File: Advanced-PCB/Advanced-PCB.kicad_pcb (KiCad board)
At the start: 2 copper layers, 24 parts, among them J1 USB_mini_micro_B, SW1 MXSwitch, SW2 MXSwitch, SW3 MXSwitch, SW4 MXSwitch, U1 ATMEGA32U4, X1 16MHz

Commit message: PCB Layout Complete
Full PCB layed out in wanted order.
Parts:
- added D10: 1N4148W, Diode_SMD:D_SOD-123, F.Cu at (11.1, 25.7)
- added D11: 1N4148W, Diode_SMD:D_SOD-123, F.Cu at (11.1, 22.4)
- added D12: 1N4148W, Diode_SMD:D_SOD-123, F.Cu at (94.6, 124.8)
- added D13: 1N4148W, Diode_SMD:D_SOD-123, F.Cu at (20.1, 57.0)
- added D14: 1N4148W, Diode_SMD:D_SOD-123, F.Cu at (31.6, 69.4)
- added D15: 1N4148W, Diode_SMD:D_SOD-123, F.Cu at (25.9, 62.7)
- added D16: 1N4148W, Diode_SMD:D_SOD-123, F.Cu at (74.5, 116.4)
- added D17: 1N4148W, Diode_SMD:D_SOD-123, F.Cu at (31.6, 66.0)
- added D18: 1N4148W, Diode_SMD:D_SOD-123, F.Cu at (31.6, 62.7)
- added D19: 1N4148W, Diode_SMD:D_SOD-123, F.Cu at (25.9, 59.3)
- added D20: 1N4148W, Diode_SMD:D_SOD-123, F.Cu at (114.8, 144.9)
- added D21: 1N4148W, Diode_SMD:D_SOD-123, F.Cu at (83.1, 118.1)
- added D22: 1N4148W, Diode_SMD:D_SOD-123, F.Cu at (88.9, 124.8)
- added D23: 1N4148W, Diode_SMD:D_SOD-123, F.Cu at (88.9, 121.4)
- added D24: 1N4148W, Diode_SMD:D_SOD-123, F.Cu at (125.4, 158.4)
- added D25: 1N4148W, Diode_SMD:D_SOD-123, F.Cu at (131.2, 161.7)
- added D26: 1N4148W, Diode_SMD:D_SOD-123, F.Cu at (20.1, 53.6)
- added D27: 1N4148W, Diode_SMD:D_SOD-123, F.Cu at (114.8, 148.3)
- added D28: 1N4148W, Diode_SMD:D_SOD-123, F.Cu at (103.3, 138.2)
- added D29: 1N4148W, Diode_SMD:D_SOD-123, F.Cu at (109.0, 144.9)
- added D30: 1N4148W, Diode_SMD:D_SOD-123, F.Cu at (94.6, 131.5)
- added D31: 1N4148W, Diode_SMD:D_SOD-123, F.Cu at (83.1, 121.4)
- added D32: 1N4148W, Diode_SMD:D_SOD-123, F.Cu at (25.4, 50.3)
- added D33: 1N4148W, Diode_SMD:D_SOD-123, F.Cu at (114.8, 141.6)
- added D34: 1N4148W, Diode_SMD:D_SOD-123, F.Cu at (109.0, 138.2)
- added D35: 1N4148W, Diode_SMD:D_SOD-123, F.Cu at (136.9, 161.7)
- added D36: 1N4148W, Diode_SMD:D_SOD-123, F.Cu at (131.2, 158.4)
- added D37: 1N4148W, Diode_SMD:D_SOD-123, F.Cu at (94.6, 121.4)
- added D38: 1N4148W, Diode_SMD:D_SOD-123, F.Cu at (114.8, 138.2)
- added D39: 1N4148W, Diode_SMD:D_SOD-123, F.Cu at (31.6, 59.3)
- added D40: 1N4148W, Diode_SMD:D_SOD-123, F.Cu at (34.2, 76.1)
- added D41: 1N4148W, Diode_SMD:D_SOD-123, F.Cu at (25.9, 56.0)
- added D42: 1N4148W, Diode_SMD:D_SOD-123, F.Cu at (54.3, 96.3)
- added D43: 1N4148W, Diode_SMD:D_SOD-123, F.Cu at (31.6, 56.0)
- added D44: 1N4148W, Diode_SMD:D_SOD-123, F.Cu at (94.6, 118.1)
- added D45: 1N4148W, Diode_SMD:D_SOD-123, F.Cu at (142.7, 161.7)
- added D46: 1N4148W, Diode_SMD:D_SOD-123, F.Cu at (136.9, 158.4)
- added D47: 1N4148W, Diode_SMD:D_SOD-123, F.Cu at (11.1, 32.4)
- added D48: 1N4148W, Diode_SMD:D_SOD-123, F.Cu at (11.1, 29.1)
- added D49: 1N4148W, Diode_SMD:D_SOD-123, F.Cu at (165.7, 158.4)
- added D5: 1N4148W, Diode_SMD:D_SOD-123, F.Cu at (20.1, 60.3)
- added D50: 1N4148W, Diode_SMD:D_SOD-123, F.Cu at (142.7, 158.4)
- added D51: 1N4148W, Diode_SMD:D_SOD-123, F.Cu at (154.2, 161.7)
- added D52: 1N4148W, Diode_SMD:D_SOD-123, F.Cu at (148.4, 158.4)
- added D53: 1N4148W, Diode_SMD:D_SOD-123, F.Cu at (11.1, 19.0)
- added D54: 1N4148W, Diode_SMD:D_SOD-123, F.Cu at (11.1, 15.7)
- added D55: 1N4148W, Diode_SMD:D_SOD-123, F.Cu at (154.2, 158.4)
- added D56: 1N4148W, Diode_SMD:D_SOD-123, F.Cu at (159.9, 161.7)
- added D57: 1N4148W, Diode_SMD:D_SOD-123, F.Cu at (165.7, 161.7)
- added D58: 1N4148W, Diode_SMD:D_SOD-123, F.Cu at (159.9, 158.4)
- added D59: 1N4148W, Diode_SMD:D_SOD-123, F.Cu at (148.4, 161.7)
- added D6: 1N4148W, Diode_SMD:D_SOD-123, F.Cu at (88.9, 128.1)
- added D60: 1N4148W, Diode_SMD:D_SOD-123, F.Cu at (181.1, 79.4)
- added D61: 1N4148W, Diode_SMD:D_SOD-123, F.Cu at (181.1, 76.0)
- added D62: 1N4148W, Diode_SMD:D_SOD-123, F.Cu at (181.1, 72.7)
- added D63: 1N4148W, Diode_SMD:D_SOD-123, F.Cu at (166.9, 52.2)
- added D64: 1N4148W, Diode_SMD:D_SOD-123, F.Cu at (181.1, 69.3)
- added D65: 1N4148W, Diode_SMD:D_SOD-123, F.Cu at (88.9, 118.1)
- added D66: 1N4148W, Diode_SMD:D_SOD-123, F.Cu at (109.0, 141.6)
- added D67: 1N4148W, Diode_SMD:D_SOD-123, F.Cu at (19.6, 50.3)
- added D7: 1N4148W, Diode_SMD:D_SOD-123, F.Cu at (94.6, 128.1)
- added D8: 1N4148W, Diode_SMD:D_SOD-123, F.Cu at (94.6, 134.8)
- added D9: 1N4148W, Diode_SMD:D_SOD-123, F.Cu at (172.7, 52.2)
- added SW10: Win 1.25, acheron_MXH:MX125H, B.Cu at (-11.9, -28.6)
- added SW11: 2, acheron_MXH:MX100H, B.Cu at (0.00, -104.8)
- added SW12: W, acheron_MXH:MX100H, B.Cu at (9.53, -85.7)
- added SW13: S, acheron_MXH:MX100H, B.Cu at (14.3, -66.7)
- added SW14: X, acheron_MXH:MX100H, B.Cu at (23.8, -47.6)
- added SW15: Alt 1.25, acheron_MXH:MX125H, B.Cu at (11.9, -28.6)
- added SW16: 3, acheron_MXH:MX100H, B.Cu at (19.1, -104.8)
- added SW17: E, acheron_MXH:MX100H, B.Cu at (28.6, -85.7)
- added SW18: D, acheron_MXH:MX100H, B.Cu at (33.3, -66.7)
- added SW19: C, acheron_MXH:MX100H, B.Cu at (42.9, -47.6)
- added SW20: 4, acheron_MXH:MX100H, B.Cu at (38.1, -104.8)
- added SW21: R, acheron_MXH:MX100H, B.Cu at (47.6, -85.7)
- added SW22: F, acheron_MXH:MX100H, B.Cu at (52.4, -66.7)
- added SW23: V, acheron_MXH:MX100H, B.Cu at (61.9, -47.6)
- added SW24: 5, acheron_MXH:MX100H, B.Cu at (57.1, -104.8)
- added SW25: T, acheron_MXH:MX100H, B.Cu at (66.7, -85.7)
- added SW26: G, acheron_MXH:MX100H, B.Cu at (71.4, -66.7)
- added SW27: B, acheron_MXH:MX100H, B.Cu at (81.0, -47.6)
- added SW28: Space 6.25, acheron_MXH:MX625HR, B.Cu at (83.3, -28.6)
- added SW29: 6, acheron_MXH:MX100H, B.Cu at (76.2, -104.8)
- added SW30: Y, acheron_MXH:MX100H, B.Cu at (85.7, -85.7)
- added SW31: H, acheron_MXH:MX100H, B.Cu at (90.5, -66.7)
- added SW32: N, acheron_MXH:MX100H, B.Cu at (100.0, -47.6)
- added SW33: 7, acheron_MXH:MX100H, B.Cu at (95.2, -104.8)
- added SW34: U, acheron_MXH:MX100H, B.Cu at (104.8, -85.7)
- added SW35: J, acheron_MXH:MX100H, B.Cu at (109.5, -66.7)
- added SW36: M, acheron_MXH:MX100H, B.Cu at (119.1, -47.6)
- added SW37: 8, acheron_MXH:MX100H, B.Cu at (114.3, -104.8)
- added SW38: I, acheron_MXH:MX100H, B.Cu at (123.8, -85.7)
- added SW39: K, acheron_MXH:MX100H, B.Cu at (128.6, -66.7)
- added SW40: ,, acheron_MXH:MX100H, B.Cu at (138.1, -47.6)
- added SW41: 9, acheron_MXH:MX100H, B.Cu at (133.3, -104.8)
- added SW42: O, acheron_MXH:MX100H, B.Cu at (161.9, -85.7)
- added SW43: L, acheron_MXH:MX100H, B.Cu at (147.6, -66.7)
- added SW44: ., acheron_MXH:MX100H, B.Cu at (157.2, -47.6)
- added SW45: Alt 1.25, acheron_MXH:MX125H, B.Cu at (154.8, -28.6)
- added SW46: 0, acheron_MXH:MX100H, B.Cu at (152.4, -104.8)
- added SW47: P, acheron_MXH:MX100H, B.Cu at (142.9, -85.7)
- added SW48: ;, acheron_MXH:MX100H, B.Cu at (166.7, -66.7)
- added SW49: /, acheron_MXH:MX100H, F.Cu at (176.2, -47.6)
- added SW5: Ctrl 1.25, acheron_MXH:MX125H, B.Cu at (-35.7, -28.6)
- added SW50: Fn 1.25, acheron_MXH:MX125H, B.Cu at (178.6, -28.6)
- added SW51: -, acheron_MXH:MX100H, B.Cu at (171.4, -104.8)
- added SW52: [, acheron_MXH:MX100H, B.Cu at (181.0, -85.7)
- added SW53: ', acheron_MXH:MX100H, B.Cu at (185.7, -66.7)
- added SW54: Shift 1.75, acheron_MXH:MX175H, B.Cu at (202.4, -47.6)
- added SW55: Left Arrow, acheron_MXH:MX100H, B.Cu at (209.6, -28.6)
- added SW56: =, acheron_MXH:MX100H, B.Cu at (190.5, -104.8)
- added SW57: ], acheron_MXH:MX100H, B.Cu at (200.0, -85.7)
- added SW58: Enter 2.25, acheron_MXH:MX225HR, B.Cu at (216.7, -66.7)
- added SW59: Up Arrow, acheron_MXH:MX100H, B.Cu at (228.6, -47.6)
- added SW6: 1, acheron_MXH:MX100H, B.Cu at (-19.1, -104.8)
- added SW60: Down Arrow, acheron_MXH:MX100H, B.Cu at (228.6, -28.6)
- added SW61: Back 2.00, acheron_MXH:MX200HR, B.Cu at (219.1, -104.8)
- added SW62: \ 1.50, acheron_MXH:MX150H, B.Cu at (223.8, -85.7)
- added SW63: Pg Up, acheron_MXH:MX100H, B.Cu at (247.7, -66.7)
- added SW64: Pg Down, acheron_MXH:MX100H, B.Cu at (247.7, -47.6)
- added SW65: Right Arrow, acheron_MXH:MX100H, B.Cu at (247.7, -28.6)
- added SW66: `, acheron_MXH:MX100H, B.Cu at (247.7, -104.8)
- added SW67: Del, acheron_MXH:MX100H, B.Cu at (247.7, -85.7)
- added SW7: Q, acheron_MXH:MX100H, B.Cu at (-9.53, -85.7)
- added SW8: A, acheron_MXH:MX100H, B.Cu at (-4.76, -66.7)
- added SW9: Z, acheron_MXH:MX100H, B.Cu at (4.76, -47.6)
- C1: value 22pF -> .1u
- C6: value .1u -> 4.7u
- C7: value 4.7u -> 22pF
- D1, D2, D3, D4: value D_Small -> 1N4148W
- R2: value 10k -> 22
- R4: value 22 -> 10k
- SW1: value MXSwitch -> Esc; moved to B.Cu
- SW2: value MXSwitch -> Tab 1.50; footprint acheron_MXH:MX100H -> acheron_MXH:MX150H; moved to B.Cu
- SW3: value MXSwitch -> Caps 1.75; footprint acheron_MXH:MX100H -> acheron_MXH:MX175H; moved to B.Cu
- SW4: value MXSwitch -> Shift 2.25; footprint acheron_MXH:MX100H -> acheron_MXH:MX225HR; moved to B.Cu
- moved SW1 182.5 mm to (-38.1, -104.8), turned to 180 degrees
- moved SWPw1 158.4 mm to (173.3, 160.2), turned to 180 degrees
- moved SW2 147.4 mm to (-33.3, -85.7), turned to 180 degrees
- moved C6 144.9 mm to (181.6, 82.5), turned to 180 degrees
- moved D2 137.8 mm to (119.7, 158.4), turned to 180 degrees
- moved SW3 135.8 mm to (-31.0, -66.7), turned to 180 degrees
- moved C7 134.9 mm to (162.0, 43.5), turned to 180 degrees
- moved D1 130.1 mm to (125.4, 161.7), turned to 180 degrees
- moved C5 119.6 mm to (161.7, 49.4), turned to 180 degrees
- moved C4 114.6 mm to (161.7, 52.4), turned to 180 degrees
- moved R1 109.7 mm to (109.5, 148.1), turned to 180 degrees
- moved X1 101.7 mm to (180.6, 64.9), turned to 180 degrees
- moved SW4 100.5 mm to (-26.2, -47.6), turned to 180 degrees
- moved J1 86.1 mm to (170.0, 42.8), turned to 180 degrees
- moved R4 85.0 mm to (11.4, 44.4), turned to 180 degrees
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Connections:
- C1 pad 1: Net-(C1-Pad1) -> VCC
- C7 pad 1: VCC -> Net-(C7-Pad1)
- D3 pad 1: Net-(D3-Pad1) -> Col1
- R2 pad 1: +5V -> Net-(R2-Pad1)
- R2 pad 2: Net-(R2-Pad2) -> Net-(J1-Pad2)
- R3 pad 2: Net-(J1-Pad2) -> Net-(J1-Pad3)
- R4 pad 1: Net-(R4-Pad1) -> +5V
- R4 pad 2: Net-(J1-Pad3) -> Net-(R4-Pad2)
- SW1 pad 2: Net-(SW1-Pad2) -> Net-(D1-Pad2)
- U1 pad 16: Net-(C1-Pad1) -> Net-(C2-Pad1)
- U1 pad 17: Net-(C2-Pad1) -> Net-(C7-Pad1)
- U1 pad 3: Net-(R3-Pad1) -> Net-(R2-Pad1)
- U1 pad 33: Net-(R2-Pad2) -> Net-(R4-Pad2)
- U1 pad 4: Net-(R4-Pad1) -> Net-(R3-Pad1)
- X1 pad 1: Net-(C1-Pad1) -> Net-(C2-Pad1)
- X1 pad 2: Net-(C2-Pad1) -> Net-(C7-Pad1)

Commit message: Alternate Row 0
Alternate Row zero with 1u right side keys added.
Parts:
- SW49: moved to B.Cu
- moved J1 165.8 mm to (104.8, -109.6)
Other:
- board outline added: 309.6 x 100 mm

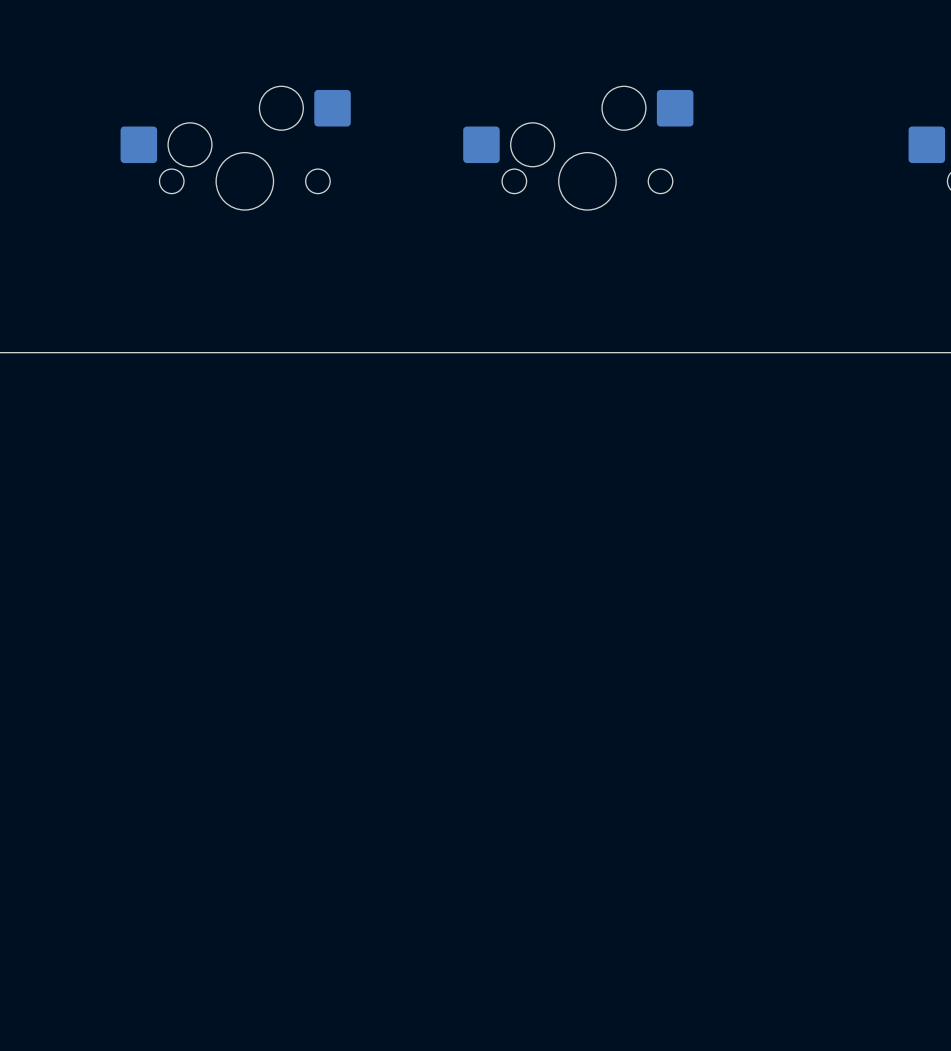
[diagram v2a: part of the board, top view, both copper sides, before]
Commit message: Layout Simplified
Layout Simplified by stacking switches unable to be used at same time because of different kb layouts. Right alt and fn with ctrl left down as seperate row.
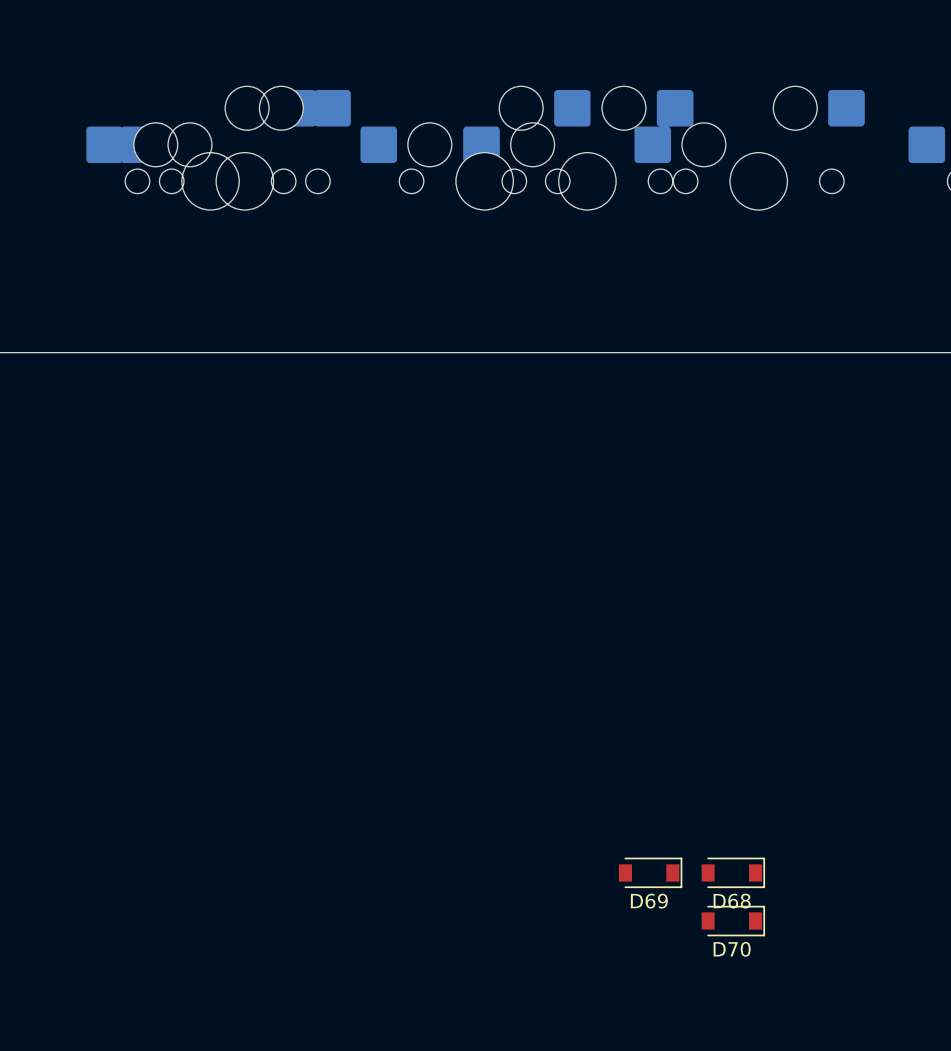
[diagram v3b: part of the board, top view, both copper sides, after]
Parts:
- added D68: 1N4148W, Diode_SMD:D_SOD-123, F.Cu at (188.6, 19.5)
- added D69: 1N4148W, Diode_SMD:D_SOD-123, F.Cu at (182.9, 19.5)
- added D70: 1N4148W, Diode_SMD:D_SOD-123, F.Cu at (188.6, 22.8)
- added SW68: Alt 1.00, acheron_MXH:MX100H, B.Cu at (152.4, -28.6)
- added SW69: Fn 1.00, acheron_MXH:MX100H, B.Cu at (171.4, -28.6)
- added SW70: Ctrl 1.00, acheron_MXH:MX100H, B.Cu at (190.5, -28.6)

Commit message: Rows And Columns Fixed
Fixed Issue to make all columns and rows linked properly
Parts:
- C1, C2, C3, C4, C5, C6, C7, C8, D1, D10, D11, D12, D13, D14, D15, D16, D17, D18, D19, D2, D20, D21, D22, D23, D24, D25, D26, D27, D28, D29, D3, D30, D31, D32, D33, D34, D35, D36, D37, D38, D39, D4, D40, D41, D42, D43, D44, D45, D46, D47, D48, D49, D5, D50, D51, D52, D53, D54, D55, D56, D57, D58, D59, D6, D60, D61, D62, D63, D64, D65, D66, D67, D68, D69, D7, D70, D8, D9, J1, R1, R2, R3, R4, SWPw1, U1, X1: moved to B.Cu
- SW1, SW11, SW12, SW13, SW14, SW16, SW17, SW18, SW19, SW20, SW21, SW22, SW23, SW24, SW25, SW26, SW27, SW29, SW30, SW31, SW32, SW33, SW34, SW35, SW36, SW37, SW38, SW39, SW40, SW41, SW43, SW44, SW46, SW48, SW49, SW51, SW52, SW53, SW55, SW56, SW57, SW59, SW6, SW60, SW63, SW64, SW65, SW66, SW67, SW68, SW69, SW7, SW70, SW8, SW9: footprint acheron_MXH:MX100H -> acheron_MXA:MXA100
- SW10, SW15, SW45, SW5, SW50: footprint acheron_MXH:MX125H -> acheron_MXA:MXA125
- SW2, SW62: footprint acheron_MXH:MX150H -> acheron_MXA:MXA150
- SW28: footprint acheron_MXH:MX625HR -> acheron_MXA:MXA625R
- SW3, SW54: footprint acheron_MXH:MX175H -> acheron_MXA:MXA175
- SW4, SW58: footprint acheron_MXH:MX225HR -> acheron_MXA:MXA225R
- SW42: value O -> P; footprint acheron_MXH:MX100H -> acheron_MXA:MXA100
- SW47: value P -> O; footprint acheron_MXH:MX100H -> acheron_MXA:MXA100
- SW61: footprint acheron_MXH:MX200HR -> acheron_MXA:MXA200R
- moved D1 308.4 mm to (-38.5, -99.6)
- moved D54 263.3 mm to (11.1, 279.0)
- moved D53 256.6 mm to (11.1, 275.6)
- moved D68 255.7 mm to (188.6, 275.1)
- moved D69 255.7 mm to (182.9, 275.1)
- moved D11 249.9 mm to (11.1, 272.3)
- moved D70 249.0 mm to (188.6, 271.8)
- moved D10 243.2 mm to (11.1, 268.9)
- moved D48 236.5 mm to (11.1, 265.6)
- moved D47 229.8 mm to (11.1, 262.2)
- moved C1 223.5 mm to (11.4, 259.1)
- moved C3 217.6 mm to (11.4, 256.1)
- moved J1 212.5 mm to (99.1, 102.9), turned to 0 degrees
- moved U1 211.9 mm to (21.0, 253.3)
- moved C2 211.7 mm to (11.4, 253.2)
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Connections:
- D1 pad 1: Col1 -> Row4
- D10 pad 1: Col1 -> Row0
- D11 pad 1: Col1 -> Row4
- D12 pad 1: Col1 -> Row3
- D13 pad 1: Col1 -> Row2
- D14 pad 1: Col1 -> Row1
- D15 pad 1: Col1 -> Row0
- D16 pad 1: Col1 -> Row4
- D17 pad 1: Col1 -> Row3
- D18 pad 1: Col1 -> Row2
- D19 pad 1: Col1 -> Row1
- D2 pad 1: Col1 -> Row3
- D20 pad 1: Col1 -> Row4
- D21 pad 1: Col1 -> Row3
- D22 pad 1: Col1 -> Row2
- D23 pad 1: Col1 -> Row1
- D24 pad 1: Col1 -> Row4
- D25 pad 1: Col1 -> Row3
- D26 pad 1: Col1 -> Row2
- D27 pad 1: Col1 -> Row1
- D28 pad 1: Col1 -> Row0
- D29 pad 1: Col1 -> Row4
- D3 pad 1: Col1 -> Row2
- D30 pad 1: Col1 -> Row3
- D31 pad 1: Col1 -> Row2
- D32 pad 1: Col1 -> Row1
- D33 pad 1: Col1 -> Row4
- D34 pad 1: Col1 -> Row3
- D35 pad 1: Col1 -> Row2
- D36 pad 1: Col1 -> Row1
- D37 pad 1: Col1 -> Row4
- D38 pad 1: Col1 -> Row3
- D39 pad 1: Col1 -> Row2
- D4 pad 1: Col1 -> Row1
- D40 pad 1: Col1 -> Row1
- D41 pad 1: Col1 -> Row4
- D42 pad 1: Col1 -> Row3
- D43 pad 1: Col1 -> Row2
- D44 pad 1: Col1 -> Row1
- D45 pad 1: Col1 -> Row0
- D46 pad 1: Col1 -> Row4
- D47 pad 1: Col1 -> Row3
- D48 pad 1: Col1 -> Row2
- D49 pad 1: Col1 -> Row1
- D5 pad 1: Col1 -> Row0
- D50 pad 1: Col1 -> Row0
- D51 pad 1: Col1 -> Row4
- D52 pad 1: Col1 -> Row3
- D53 pad 1: Col1 -> Row2
- D54 pad 1: Col1 -> Row1
- D55 pad 1: Col1 -> Row0
- D56 pad 1: Col1 -> Row4
- D57 pad 1: Col1 -> Row3
- D58 pad 1: Col1 -> Row2
- D59 pad 1: Col1 -> Row1
- D6 pad 1: Col1 -> Row4
- D60 pad 1: Col1 -> Row0
- D61 pad 1: Col1 -> Row4
- D62 pad 1: Col1 -> Row3
- D63 pad 1: Col1 -> Row2
- D64 pad 1: Col1 -> Row1
- D65 pad 1: Col1 -> Row0
- D66 pad 1: Col1 -> Row4
- D67 pad 1: Col1 -> Row3
- D7 pad 1: Col1 -> Row3
- D70 pad 1: Col1 -> Row0
- D8 pad 1: Col1 -> Row2
- D9 pad 1: Col1 -> Row1
- SW10 pad 1: Col1 -> Col2
- SW11 pad 1: Col1 -> Col3
- SW12 pad 1: Col1 -> Col3
- SW13 pad 1: Col1 -> Col3
- SW14 pad 1: Col1 -> Col3
- SW15 pad 1: Col1 -> Col3
- SW16 pad 1: Col1 -> Col4
- SW17 pad 1: Col1 -> Col4
- SW18 pad 1: Col1 -> Col4
- SW19 pad 1: Col1 -> Col4
- SW20 pad 1: Col1 -> Col5
- SW21 pad 1: Col1 -> Col5
- SW22 pad 1: Col1 -> Col5
- SW23 pad 1: Col1 -> Col5
- SW24 pad 1: Col1 -> Col6
- SW25 pad 1: Col1 -> Col6
- SW26 pad 1: Col1 -> Col6
- SW27 pad 1: Col1 -> Col6
- SW28 pad 1: Col1 -> Col6
- SW29 pad 1: Col1 -> Col7
- SW30 pad 1: Col1 -> Col7
- SW31 pad 1: Col1 -> Col7
- SW32 pad 1: Col1 -> Col7
- SW33 pad 1: Col1 -> Col8
- SW34 pad 1: Col1 -> Col8
- SW35 pad 1: Col1 -> Col8
- SW36 pad 1: Col1 -> Col8
- SW37 pad 1: Col1 -> Col9
- SW38 pad 1: Col1 -> Col9
- SW39 pad 1: Col1 -> Col9
- SW40 pad 1: Col1 -> Col9
- SW41 pad 1: Col1 -> Col10
- SW42 pad 1: Col1 -> Col10
- SW43 pad 1: Col1 -> Col10
- SW44 pad 1: Col1 -> Col10
- SW45 pad 1: Col1 -> Col10
- SW46 pad 1: Col1 -> Col11
- SW47 pad 1: Col1 -> Col11
- SW48 pad 1: Col1 -> Col11
- SW49 pad 1: Col1 -> Col11
- SW50 pad 1: Col1 -> Col11
- SW51 pad 1: Col1 -> Col12
- SW52 pad 1: Col1 -> Col12
- SW53 pad 1: Col1 -> Col12
- SW54 pad 1: Col1 -> Col12
- SW55 pad 1: Col1 -> Col12
- SW56 pad 1: Col1 -> Col13
- SW57 pad 1: Col1 -> Col13
- SW58 pad 1: Col1 -> Col13
- SW59 pad 1: Col1 -> Col13
- SW6 pad 1: Col1 -> Col2
- SW60 pad 1: Col1 -> Col13
- SW61 pad 1: Col1 -> Col14
- SW62 pad 1: Col1 -> Col14
- SW63 pad 1: Col1 -> Col14
- SW64 pad 1: Col1 -> Col14
- SW65 pad 1: Col1 -> Col14
- SW66 pad 1: Col1 -> Col15
- SW67 pad 1: Col1 -> Col15
- SW68 pad 1: Net-(SW68-Pad1) -> Col10
- SW68 pad 2: Net-(SW68-Pad2) -> Net-(D45-Pad2)
- SW69 pad 1: Col1 -> Col11
- SW69 pad 2: Net-(D69-Pad2) -> Net-(D50-Pad2)
- SW7 pad 1: Col1 -> Col2
- SW70 pad 1: Col1 -> Col12
- SW8 pad 1: Col1 -> Col2
- SW9 pad 1: Col1 -> Col2
- U1 pad 11: Net-(U1-Pad11) -> Col10
- U1 pad 18: Net-(U1-Pad18) -> Col11
- U1 pad 19: Net-(U1-Pad19) -> Col12
- U1 pad 20: Net-(U1-Pad20) -> Col13
- U1 pad 21: Net-(U1-Pad21) -> Col14
- U1 pad 22: Net-(U1-Pad22) -> Col15
- U1 pad 25: Net-(U1-Pad25) -> Col9
- U1 pad 26: Net-(U1-Pad26) -> Col8
- U1 pad 27: Net-(U1-Pad27) -> Col7
- U1 pad 28: Net-(U1-Pad28) -> Col6
- U1 pad 29: Net-(U1-Pad29) -> Col5
- U1 pad 30: Net-(U1-Pad30) -> Col4
- U1 pad 31: Net-(U1-Pad31) -> Col3
- U1 pad 32: Net-(U1-Pad32) -> Col2
- U1 pad 36: Net-(U1-Pad36) -> Col1
- U1 pad 37: Net-(U1-Pad37) -> Row4
- U1 pad 38: Col1 -> Row3
- U1 pad 39: Col1 -> Row2
- U1 pad 40: Col1 -> Row1
- U1 pad 41: Col1 -> Row0

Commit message: Mid Routing
In the Middle of Routing. All of tracing between initial components done. Switches still need to be traced and connected.
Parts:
- removed D68, D69: 1N4148W, Diode_SMD:D_SOD-123
- X1: value 16MHz -> XTAL_GND; footprint Crystal:Crystal_SMD_SeikoEpson_TSX3225-4Pin_3.2x2.5mm_HandSoldering -> kicad-library-master:crystal_FA238-TSX3225
- moved D67 397.2 mm to (247.9, -80.7)
- moved C7 384.8 mm to (-16.0, -90.0), turned to 270 degrees
- moved C5 384.2 mm to (-27.5, -89.2), turned to 90 degrees
- moved D53 379.9 mm to (185.9, -61.6)
- moved C8 379.0 mm to (-28.9, -79.2), turned to 90 degrees
- moved X1 376.8 mm to (-20.0, -89.2), turned to 45 degrees
- moved C4 376.4 mm to (-27.3, -83.2), turned to 45 degrees
- moved D47 374.7 mm to (162.2, -80.7)
- moved D54 374.3 mm to (202.7, -42.5)
- moved D11 372.1 mm to (0.30, -99.7)
- moved D48 362.4 mm to (166.9, -61.6)
- moved C6 356.4 mm to (-28.5, -75.7), turned to 175 degrees
- moved D41 355.1 mm to (133.6, -99.7)
- moved C2 345.0 mm to (-24.4, -90.0), turned to 270 degrees
- moved R3 343.1 mm to (-18.8, -94.5), turned to 0 degrees
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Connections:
- net +5V renamed GND
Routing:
- net Row3: track 0.00 -> 366.4 mm, vias 0 -> 4
- net Row0: track 0.00 -> 361.7 mm
- net Row4: track 0.00 -> 346.6 mm, vias 0 -> 2
- net Row2: track 0.00 -> 345.4 mm
- net Row1: track 0.00 -> 325.5 mm
- net VCC: track 0.00 -> 143.5 mm
- net Col12: track 0.00 -> 109.7 mm
- net Col2: track 0.00 -> 103.4 mm
- net Col11: track 0.00 -> 97.3 mm
- net Col13: track 0.00 -> 94.6 mm
- net Col14: track 0.00 -> 92.7 mm
- net Col10: track 0.00 -> 90.6 mm
- net Col9: track 0.00 -> 69.7 mm
- net Col8: track 0.00 -> 69.7 mm
- net Col1: track 0.00 -> 66.7 mm
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- added copper zone on B.Cu, net GND
- added copper zone on F.Cu, net GND
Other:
- net class Default: trace_width 0.25 -> 0.254
- net class Power added: clearance 0.2, trace_width 0.381, via_dia 0.8, via_drill 0.4

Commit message: Traces Continued
Continued Tracing All Rows and Half Columns completed.
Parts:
- moved C1 2.13 mm to (-12.2, -69.0), turned to 225 degrees
- moved R4 0.30 mm to (-10.2, -72.8)
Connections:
- U1 pad 11: Col10 -> Col1
- U1 pad 18: Col11 -> Col15
- U1 pad 19: Col12 -> Col14
- U1 pad 21: Col14 -> Col12
- U1 pad 22: Col15 -> Col11
- U1 pad 25: Col9 -> Col3
- U1 pad 26: Col8 -> Col4
- U1 pad 27: Col7 -> Col5
- U1 pad 29: Col5 -> Col7
- U1 pad 30: Col4 -> Col8
- U1 pad 31: Col3 -> Col9
- U1 pad 32: Col2 -> Col10
- U1 pad 36: Col1 -> Col2
- U1 pad 40: Row1 -> Row0
- U1 pad 41: Row0 -> Row1
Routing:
- net Col15: track 19.0 -> 339.2 mm, vias 0 -> 2
- net Col14: track 92.7 -> 406.2 mm, vias 0 -> 3
- net Col13: track 94.6 -> 357.6 mm, vias 0 -> 3
- net Col12: track 109.7 -> 352.4 mm, vias 0 -> 3
- net Col11: track 97.3 -> 319.5 mm, vias 0 -> 3
- net Col10: track 90.6 -> 263.6 mm, vias 0 -> 17
- net Col9: track 69.7 -> 221.9 mm, vias 0 -> 15
- net Col8: track 69.7 -> 202.0 mm, vias 0 -> 14
- net Col6: track 0.00 -> 105.5 mm, vias 0 -> 1
- net Col3: track 0.00 -> 97.0 mm
- net Col7: track 0.00 -> 91.0 mm, vias 0 -> 1
- net Col4: track 0.00 -> 85.3 mm, vias 0 -> 1
- net Col5: track 0.00 -> 84.4 mm, vias 0 -> 1
- net Row4: track 346.6 -> 391.9 mm, vias 2 -> 4
- net Row1: track 325.5 -> 365.4 mm, vias 0 -> 4
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
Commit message: PCB-Rerouted
Correctly Rerouted and except of errors except for with layer keys.
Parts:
- SW45, SW50: footprint acheron_MXA:MXA125 -> acheron_MX:MX125
- SW68, SW69: footprint acheron_MXA:MXA100 -> acheron_MX:MX100
- moved C5 317.6 mm to (190.2, 142.1), turned to 270 degrees
- moved C4 311.4 mm to (187.6, 142.1), turned to 270 degrees
- moved C3 293.0 mm to (184.6, 142.1)
- moved C8 289.1 mm to (159.0, 140.5), turned to 180 degrees
- moved R4 287.6 mm to (184.8, 138.7), turned to 180 degrees
- moved C2 286.7 mm to (168.8, 121.9)
- moved C7 286.6 mm to (177.0, 121.9)
- moved C1 286.4 mm to (181.4, 142.1), turned to 270 degrees
- moved X1 286.2 mm to (173.4, 121.7)
- moved U1 285.1 mm to (172.8, 135.5)
- moved C6 278.6 mm to (166.0, 123.7), turned to 90 degrees
- moved SWPw1 266.1 mm to (159.0, 135.1), turned to 270 degrees
- moved R1 265.9 mm to (159.2, 129.1), turned to 0 degrees
- moved D59 173.3 mm to (292.4, 118.7)
- moved D60 173.3 mm to (292.4, 137.8)
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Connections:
- SW46 pad 2: Net-(SW46-Pad2) -> Net-(D46-Pad2)
- U1 pad 11: Col1 -> Col6
- U1 pad 18: Col15 -> Net-(U1-Pad18)
- U1 pad 19: Col14 -> Row4
- U1 pad 20: Col13 -> Row3
- U1 pad 21: Col12 -> Row2
- U1 pad 22: Col11 -> Row1
- U1 pad 25: Col3 -> Col11
- U1 pad 26: Col4 -> Col12
- U1 pad 27: Col5 -> Col13
- U1 pad 28: Col6 -> Col14
- U1 pad 29: Col7 -> Col15
- U1 pad 30: Col8 -> Col10
- U1 pad 32: Col10 -> Col8
- U1 pad 36: Col2 -> Col7
- U1 pad 37: Row4 -> Col5
- U1 pad 38: Row3 -> Col4
- U1 pad 39: Row2 -> Col3
- U1 pad 40: Row0 -> Col2
- U1 pad 41: Row1 -> Col1
- U1 pad 42: Net-(U1-Pad42) -> Row0
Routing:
- net Col2: track 130.2 -> 778.4 mm, vias 1 -> 0
- net Col7: track 91.0 -> 477.9 mm, vias 1 -> 0
- net Col5: track 84.4 -> 433.7 mm, vias 1 -> 0
- net GND: track 46.3 -> 376.7 mm, vias 6 -> 13
- net Col4: track 85.3 -> 412.5 mm, vias 1 -> 0
- net Col3: track 97.0 -> 423.5 mm
- net Col8: track 202.0 -> 505.1 mm, vias 14 -> 2
- net Col9: track 221.9 -> 484.4 mm, vias 15 -> 2
- net Col1: track 102.9 -> 361.3 mm, vias 1 -> 2
- net Net-(R3-Pad1): track 24.5 -> 252.4 mm
- net Col10: track 263.6 -> 490.9 mm, vias 17 -> 2
- net Net-(R2-Pad1): track 25.1 -> 251.2 mm
- net VCC: track 144.5 -> 341.8 mm
- net Col14: track 406.2 -> 273.5 mm, vias 3 -> 2
- net Col11: track 319.5 -> 191.6 mm, vias 3 -> 4
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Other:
- board size 309.6 x 100 mm -> 318.9 x 109.4 mm
- board text added: "Here"
